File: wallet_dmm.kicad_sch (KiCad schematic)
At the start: 13 parts, among them J1 Conn_01x04, SW1 REST_BUTTON, U1 TLC555xD, U2 STM32L051K8Tx

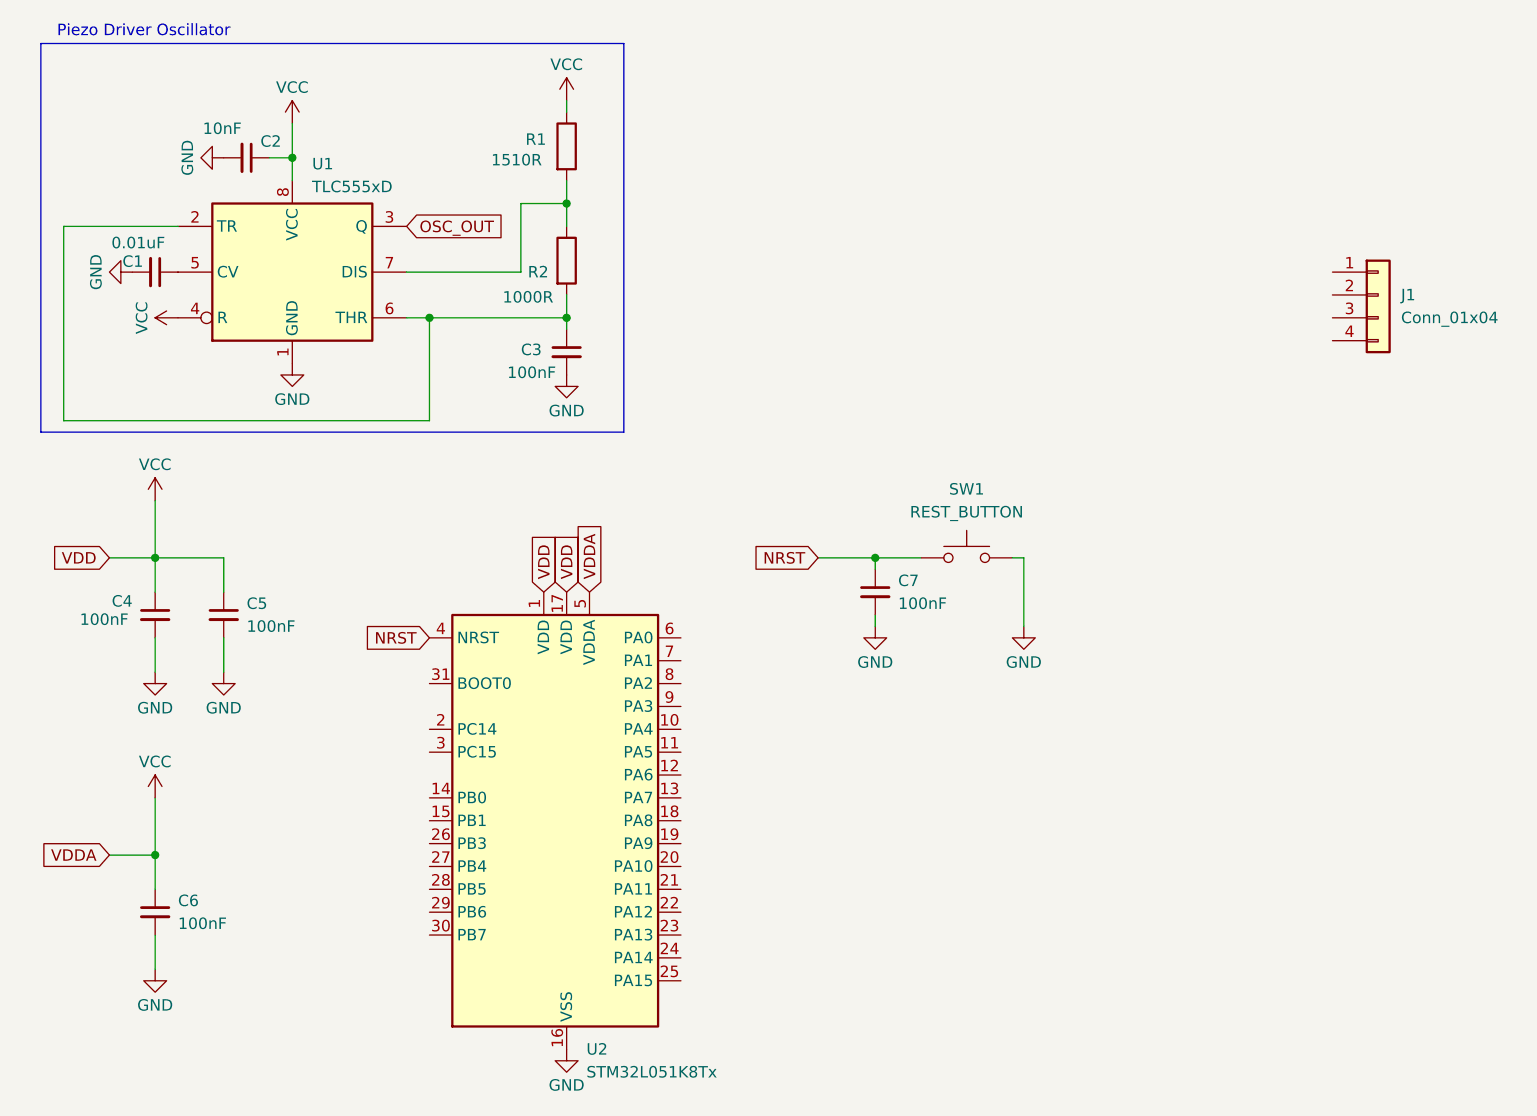
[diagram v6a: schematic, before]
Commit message: Added boot configuration jumper (default low) and I2C connector.
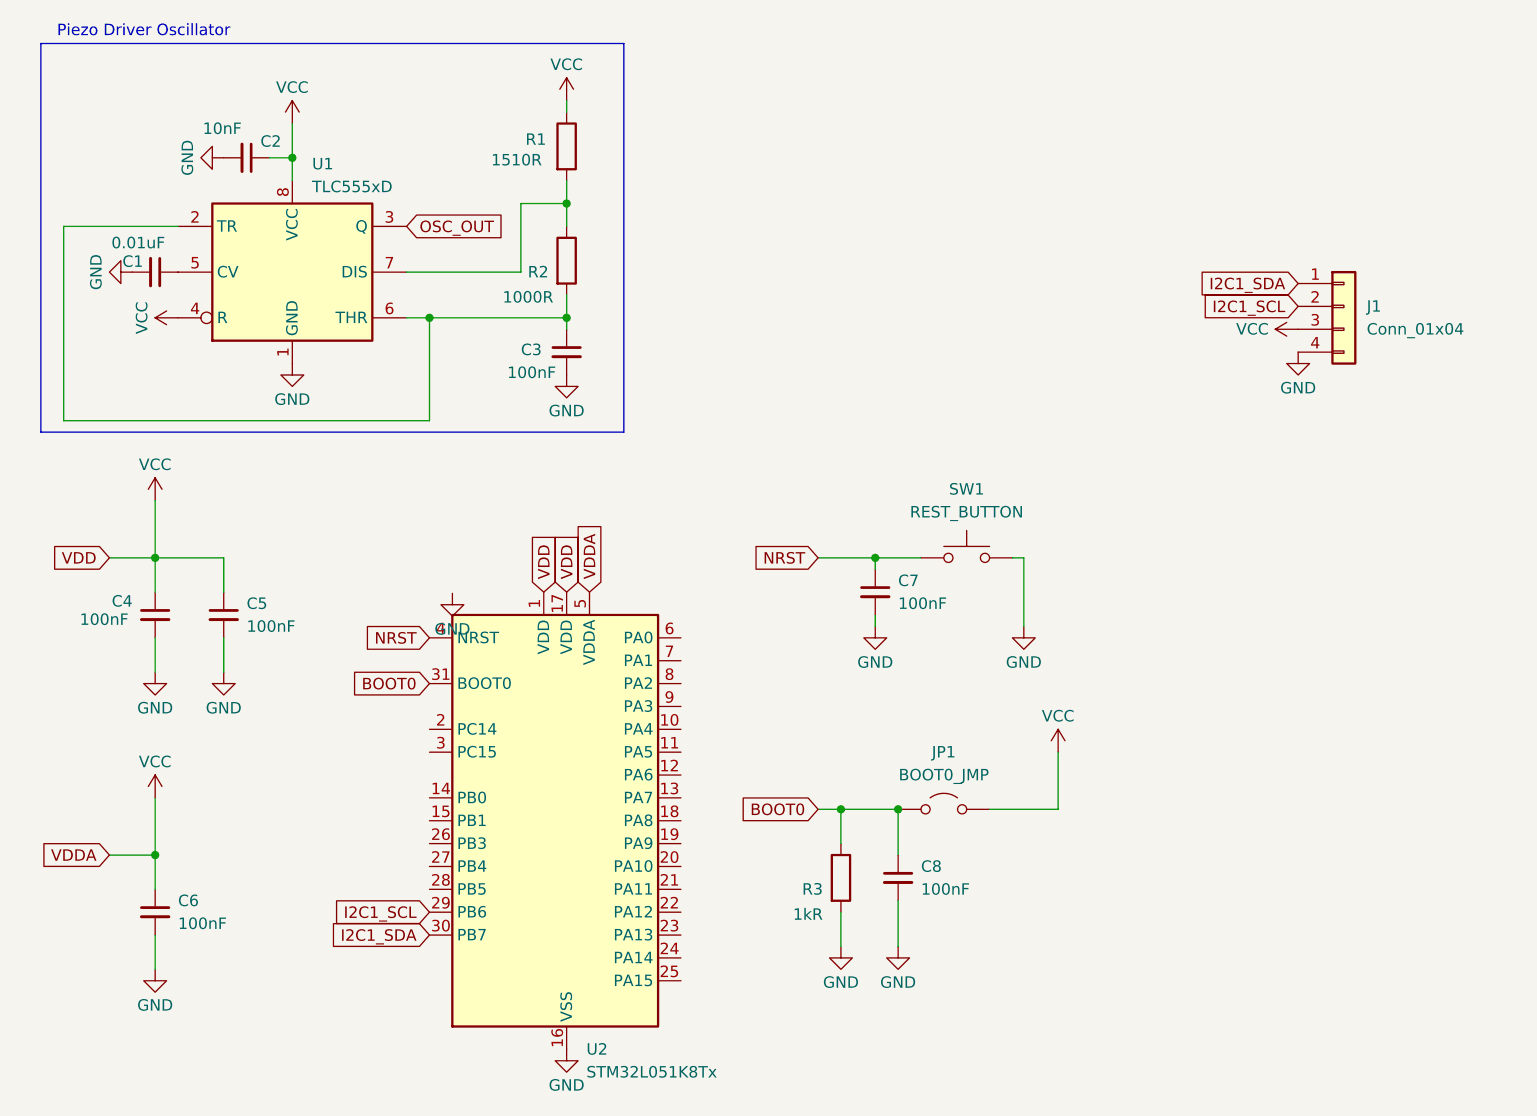
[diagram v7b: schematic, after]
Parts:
- added C8: 100nF, symbol Device:C_Small
- added JP1: BOOT0_JMP, symbol Jumper:Jumper_2_Open
- added R3: 1kR, symbol Device:R
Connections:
- net GND: now also J1.4 (Pin_4), C8.2, R3.2
- net VCC: now also J1.3 (Pin_3), JP1.2 (B)
- net I2C1_SCL: now reaches U2.29 (PB6)
- net I2C1_SCL: now also J1.2 (Pin_2)
- net I2C1_SDA: now reaches U2.30 (PB7)
- net I2C1_SDA: now also J1.1 (Pin_1)
- net BOOT0: now reaches U2.31 (BOOT0)
- net BOOT0: now also C8.1, JP1.1 (A), R3.1
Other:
- moved on the sheet: J1

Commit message: saving work
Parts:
- JP1: footprint (none) -> Jumper:SolderJumper-2_P1.3mm_Open_RoundedPad1.0x1.5mm
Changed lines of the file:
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@@
 			)
 		)
-		(property "Footprint" ""
+		(property "Footprint" "Jumper:SolderJumper-2_P1.3mm_Open_RoundedPad1.0x1.5mm"
 			(at 114.3 101.6 0)
 			(effects
